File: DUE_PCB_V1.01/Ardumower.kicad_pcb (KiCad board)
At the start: 2 copper layers, 169.3 x 95.5 mm, 81 parts, among them J1 I2C_1, J10 Bumper Left, J11 Bumper Right, J12 P_Left, J13 P_Right, J14 Sonar_R, J15 Sonar_C, J16 Sonar_L, J17 US1, J18 US2, J19 US3, J2 I2C_2, J20 Button, J21 5V IN, J22 Remote, J23 PCB_2, J24 3.3V IN, J25 TX0/RX0, J26 TX1/RX1, J27 TX2/RX2, J28 GPS_TX/GPS_RX, J29 Motor Left, J3 I2C_3, J30 Cutter Motor, J31 Motor Right, J4 DS3231 RTC, J5 9V IN, J6 Drop_Left, J7 Drop_Right, J8 Tilt, J9 Rain, U1 MC33926, U2 MC33926

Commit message: Change D6 and D7
Add Description for PIN D6 and D7 to pinFrontMotorLeft and pinFrontMotorRight
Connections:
- XA1 pad D6: pinFrontMotorLeft -> (no net)
- XA1 pad D7: pinFrontMotorLeft -> (no net)
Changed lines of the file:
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@@
     (zones 0)
     (modules 81)
-    (nets 94)
+    (nets 93)
   )
   (page A4)
@@
   (net 82 DUE_3.3V)
   (net 83 DUE_5V)
-  (net 84 pinFrontMotorLeft)
-  (net 85 "Net-(D3-Pad2)")
-  (net 86 "Net-(J15-Pad3)")
-  (net 87 "Net-(J16-Pad3)")
-  (net 88 "Net-(J21-Pad2)")
-  (net 89 "Net-(J24-Pad2)")
-  (net 90 "Net-(J31-Pad6)")
-  (net 91 "Net-(J31-Pad4)")
-  (net 92 "Net-(J31-Pad1)")
-  (net 93 "Net-(JP3-Pad2)")
+  (net 84 "Net-(D3-Pad2)")
+  (net 85 "Net-(J15-Pad3)")
+  (net 86 "Net-(J16-Pad3)")
+  (net 87 "Net-(J21-Pad2)")
+  (net 88 "Net-(J24-Pad2)")
+  (net 89 "Net-(J31-Pad6)")
+  (net 90 "Net-(J31-Pad4)")
+  (net 91 "Net-(J31-Pad1)")
+  (net 92 "Net-(JP3-Pad2)")
   (net_class Default "This is the default net class."
     (clearance 0.2)
@@
     (add_net pinDropRight)
     (add_net pinFrontMotorLeft)
+    (add_net pinFrontMotorRight)
     (add_net pinLED)
     (add_net pinLawnBackRecv)
@@
       (net 40 pinSonarCenterTrigger))
     (pad 3 thru_hole oval (at 0 5.08) (size 1.7 1.7) (drill 1) (layers *.Cu *.Mask)
-      (net 86 "Net-(J15-Pad3)"))
+      (net 85 "Net-(J15-Pad3)"))
     (pad 2 thru_hole oval (at 0 2.54) (size 1.7 1.7) (drill 1) (layers *.Cu *.Mask)
       (net 3 GND))
@@
     (fp_line (start 7.79 4) (end -2.71 4) (layer F.CrtYd) (width 0.05))
     (pad 2 thru_hole circle (at 5.08 0 90) (size 3 3) (drill 1.52) (layers *.Cu *.Mask)
-      (net 88 "Net-(J21-Pad2)"))
+      (net 87 "Net-(J21-Pad2)"))
     (pad 1 thru_hole rect (at 0 0 90) (size 3 3) (drill 1.52) (layers *.Cu *.Mask)
       (net 3 GND))
@@
     (fp_line (start 7.79 4) (end -2.71 4) (layer F.CrtYd) (width 0.05))
     (pad 2 thru_hole circle (at 5.08 0 90) (size 3 3) (drill 1.52) (layers *.Cu *.Mask)
-      (net 89 "Net-(J24-Pad2)"))
+      (net 88 "Net-(J24-Pad2)"))
     (pad 1 thru_hole rect (at 0 0 90) (size 3 3) (drill 1.52) (layers *.Cu *.Mask)
       (net 3 GND))
@@
     )
     (pad 2 thru_hole oval (at 0 2.54) (size 1.7 1.7) (drill 1) (layers *.Cu *.Mask)
-      (net 93 "Net-(JP3-Pad2)"))
+      (net 92 "Net-(JP3-Pad2)"))
     (pad 1 thru_hole rect (at 0 0) (size 1.7 1.7) (drill 1) (layers *.Cu *.Mask)
       (net 27 pinBuzzer))
@@
     )
     (pad 2 thru_hole oval (at 0 2.54) (size 1.7 1.7) (drill 1) (layers *.Cu *.Mask)
-      (net 92 "Net-(J31-Pad1)"))
+      (net 91 "Net-(J31-Pad1)"))
     (pad 1 thru_hole rect (at 0 0) (size 1.7 1.7) (drill 1) (layers *.Cu *.Mask)
       (net 68 +5VA))
@@
       (net 80 +3V3))
     (pad 1 thru_hole rect (at 0 0) (size 1.7 1.7) (drill 1) (layers *.Cu *.Mask)
-      (net 89 "Net-(J24-Pad2)"))
+      (net 88 "Net-(J24-Pad2)"))
     (model ${KISYS3DMOD}/Connector_PinHeader_2.54mm.3dshapes/PinHeader_1x03_P2.54mm_Vertical.wrl
       (at (xyz 0 0 0))
@@
       (net 81 +5V))
     (pad 1 thru_hole rect (at 0 0) (size 1.7 1.7) (drill 1) (layers *.Cu *.Mask)
-      (net 88 "Net-(J21-Pad2)"))
+      (net 87 "Net-(J21-Pad2)"))
     (model ${KISYS3DMOD}/Connector_PinHeader_2.54mm.3dshapes/PinHeader_1x03_P2.54mm_Vertical.wrl
       (at (xyz 0 0 0))
@@
       (net 8 pinMotorRightPWM))
     (pad 6 thru_hole oval (at -2.54 5.08) (size 1.7 1.7) (drill 1) (layers *.Cu *.Mask)
-      (net 90 "Net-(J31-Pad6)"))
+      (net 89 "Net-(J31-Pad6)"))
     (pad 5 thru_hole oval (at 0 5.08) (size 1.7 1.7) (drill 1) (layers *.Cu *.Mask)
       (net 67 MotorBreak))
     (pad 4 thru_hole oval (at -2.54 2.54) (size 1.7 1.7) (drill 1) (layers *.Cu *.Mask)
-      (net 91 "Net-(J31-Pad4)"))
+      (net 90 "Net-(J31-Pad4)"))
     (pad 3 thru_hole oval (at 0 2.54) (size 1.7 1.7) (drill 1) (layers *.Cu *.Mask)
       (net 10 pinMotorRightDir))
@@
       (net 9 pinMotorEnable))
     (pad 1 thru_hole rect (at 0 0) (size 1.7 1.7) (drill 1) (layers *.Cu *.Mask)
-      (net 92 "Net-(J31-Pad1)"))
+      (net 91 "Net-(J31-Pad1)"))
     (model ${KISYS3DMOD}/Connector_PinSocket_2.54mm.3dshapes/PinSocket_2x04_P2.54mm_Vertical.wrl
       (at (xyz 0 0 0))
@@
       (net 37 pinSonarLeftTrigger))
     (pad 3 thru_hole oval (at 0 5.08) (size 1.7 1.7) (drill 1) (layers *.Cu *.Mask)
-      (net 87 "Net-(J16-Pad3)"))
+      (net 86 "Net-(J16-Pad3)"))
     (pad 2 thru_hole oval (at 0 2.54) (size 1.7 1.7) (drill 1) (layers *.Cu *.Mask)
       (net 3 GND))
@@
       (net 6 pinMotorRightFault))
     (pad 1 thru_hole circle (at 0 0) (size 1.6 1.6) (drill 0.8) (layers *.Cu *.Mask)
-      (net 90 "Net-(J31-Pad6)"))
+      (net 89 "Net-(J31-Pad6)"))
     (model ${KISYS3DMOD}/Resistor_THT.3dshapes/R_Axial_DIN0207_L6.3mm_D2.5mm_P2.54mm_Vertical.wrl
       (at (xyz 0 0 0))
@@
       (net 3 GND))
     (pad 1 thru_hole circle (at 0 0) (size 1.6 1.6) (drill 0.8) (layers *.Cu *.Mask)
-      (net 90 "Net-(J31-Pad6)"))
+      (net 89 "Net-(J31-Pad6)"))
     (model ${KISYS3DMOD}/Resistor_THT.3dshapes/R_Axial_DIN0207_L6.3mm_D2.5mm_P2.54mm_Vertical.wrl
       (at (xyz 0 0 0))
@@
       (net 20 pinOdometryRight))
     (pad 1 thru_hole circle (at 0 0) (size 1.6 1.6) (drill 0.8) (layers *.Cu *.Mask)
-      (net 91 "Net-(J31-Pad4)"))
+      (net 90 "Net-(J31-Pad4)"))
     (model ${KISYS3DMOD}/Resistor_THT.3dshapes/R_Axial_DIN0207_L6.3mm_D2.5mm_P2.54mm_Vertical.wrl
       (at (xyz 0 0 0))
@@
       (net 3 GND))
     (pad 1 thru_hole circle (at 0 0) (size 1.6 1.6) (drill 0.8) (layers *.Cu *.Mask)
-      (net 91 "Net-(J31-Pad4)"))
+      (net 90 "Net-(J31-Pad4)"))
     (model ${KISYS3DMOD}/Resistor_THT.3dshapes/R_Axial_DIN0207_L6.3mm_D2.5mm_P2.54mm_Vertical.wrl
       (at (xyz 0 0 0))
@@
     (fp_arc (start 1.27 0) (end -0.23 -1.16619) (angle 284.3) (layer F.Fab) (width 0.1))
     (pad 2 thru_hole circle (at 2.54 0 270) (size 1.8 1.8) (drill 0.9) (layers *.Cu *.Mask)
-      (net 85 "Net-(D3-Pad2)"))
+      (net 84 "Net-(D3-Pad2)"))
     (pad 1 thru_hole rect (at 0 0 270) (size 1.8 1.8) (drill 0.9) (layers *.Cu *.Mask)
       (net 3 GND))
@@
     (pad GND1 thru_hole oval (at 26.416 -50.8) (size 1.7272 1.7272) (drill 1.016) (layers *.Cu *.Mask)
       (net 3 GND))
-    (pad D7 thru_hole oval (at 45.72 -50.8) (size 1.7272 1.7272) (drill 1.016) (layers *.Cu *.Mask)
-      (net 84 pinFrontMotorLeft))
-    (pad D6 thru_hole oval (at 48.26 -50.8) (size 1.7272 1.7272) (drill 1.016) (layers *.Cu *.Mask)
-      (net 84 pinFrontMotorLeft))
+    (pad D7 thru_hole oval (at 45.72 -50.8) (size 1.7272 1.7272) (drill 1.016) (layers *.Cu *.Mask))
+    (pad D6 thru_hole oval (at 48.26 -50.8) (size 1.7272 1.7272) (drill 1.016) (layers *.Cu *.Mask))
     (pad D5 thru_hole oval (at 50.8 -50.8) (size 1.7272 1.7272) (drill 1.016) (layers *.Cu *.Mask)
       (net 13 pinMotorLeftPWM))
@@
       (net 3 GND))
     (pad 2 thru_hole circle (at 3.79984 0 270) (size 2 2) (drill 1.00076) (layers *.Cu *.Mask F.SilkS)
-      (net 93 "Net-(JP3-Pad2)"))
+      (net 92 "Net-(JP3-Pad2)"))
     (model ${KISYS3DMOD}/Buzzers_Beepers.3dshapes/Buzzer_12x9.5RM7.6.wrl
       (at (xyz 0 0 0))
@@
       (net 80 +3V3))
     (pad 1 thru_hole circle (at 0 0) (size 1.6 1.6) (drill 0.8) (layers *.Cu *.Mask)
-      (net 85 "Net-(D3-Pad2)"))
+      (net 84 "Net-(D3-Pad2)"))
     (model ${KISYS3DMOD}/Resistor_THT.3dshapes/R_Axial_DIN0207_L6.3mm_D2.5mm_P2.54mm_Vertical.wrl
       (at (xyz 0 0 0))
@@
       (net 3 GND))
     (pad 1 thru_hole circle (at 0 0 270) (size 1.6 1.6) (drill 0.8) (layers *.Cu *.Mask)
-      (net 87 "Net-(J16-Pad3)"))
+      (net 86 "Net-(J16-Pad3)"))
     (model ${KISYS3DMOD}/Resistor_THT.3dshapes/R_Axial_DIN0207_L6.3mm_D2.5mm_P2.54mm_Vertical.wrl
       (at (xyz 0 0 0))
@@
       (net 3 GND))
     (pad 1 thru_hole circle (at 0 0 90) (size 1.6 1.6) (drill 0.8) (layers *.Cu *.Mask)
-      (net 86 "Net-(J15-Pad3)"))
+      (net 85 "Net-(J15-Pad3)"))
     (model ${KISYS3DMOD}/Resistor_THT.3dshapes/R_Axial_DIN0207_L6.3mm_D2.5mm_P2.54mm_Vertical.wrl
       (at (xyz 0 0 0))
@@
       (net 35 pinSonarLeftEcho))
     (pad 1 thru_hole circle (at 0 0 90) (size 1.6 1.6) (drill 0.8) (layers *.Cu *.Mask)
-      (net 87 "Net-(J16-Pad3)"))
+      (net 86 "Net-(J16-Pad3)"))
     (model ${KISYS3DMOD}/Resistor_THT.3dshapes/R_Axial_DIN0207_L6.3mm_D2.5mm_P2.54mm_Vertical.wrl
       (at (xyz 0 0 0))
@@
       (net 41 pinSonarCenterEcho))
     (pad 1 thru_hole circle (at 0 0 270) (size 1.6 1.6) (drill 0.8) (layers *.Cu *.Mask)
-      (net 86 "Net-(J15-Pad3)"))
+      (net 85 "Net-(J15-Pad3)"))
     (model ${KISYS3DMOD}/Resistor_THT.3dshapes/R_Axial_DIN0207_L6.3mm_D2.5mm_P2.54mm_Vertical.wrl
       (at (xyz 0 0 0))

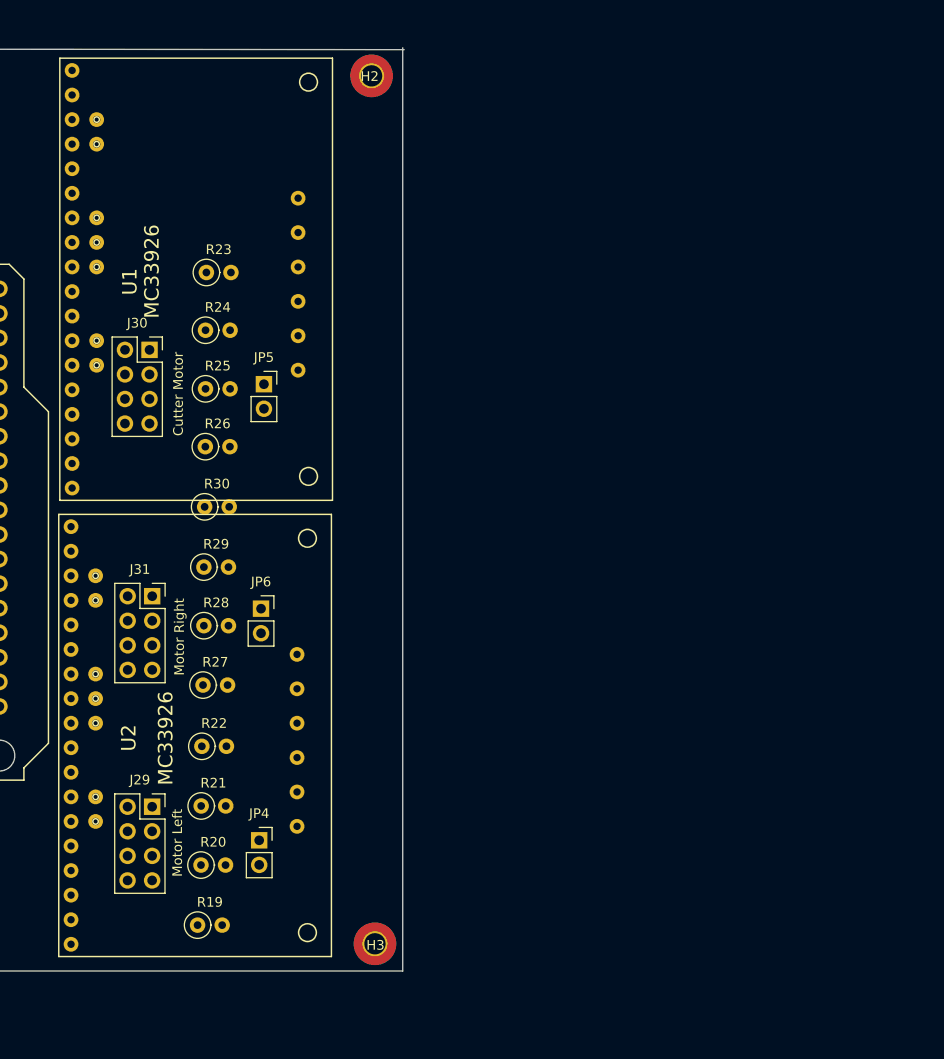
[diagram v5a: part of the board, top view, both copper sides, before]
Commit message: Add new Connectors for 4 Mow Motors and Odometrie
Add new Connectors for 4 Mow Motors and Odometrie
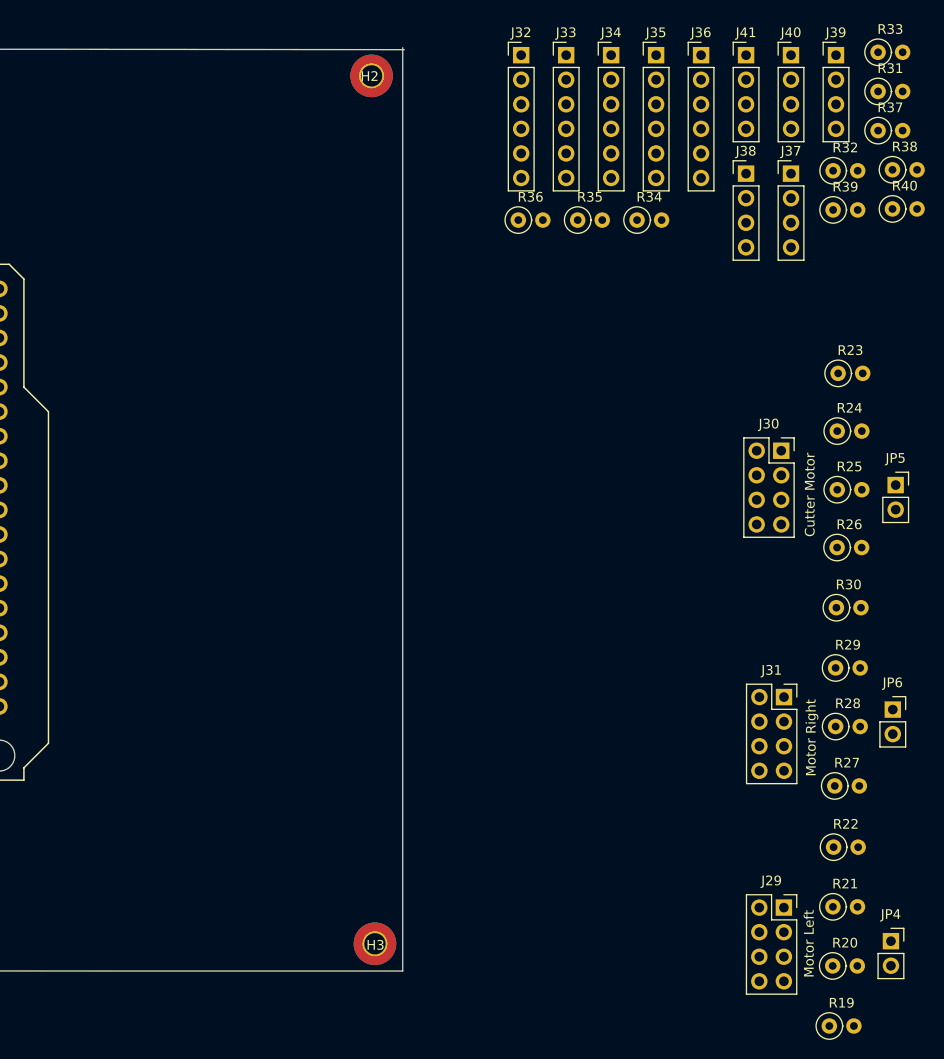
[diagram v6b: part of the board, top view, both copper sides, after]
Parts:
- removed U1, U2: MC33926, Zimprich:MC_33926_31polig_mit_Bohrloch_neue_Masse
- added J32: Motor_Right1, Connector_PinHeader_2.54mm:PinHeader_1x06_P2.54mm_Vertical, F.Cu at (220.6, 36.2)
- added J33: Motor_Right2, Connector_PinHeader_2.54mm:PinHeader_1x06_P2.54mm_Vertical, F.Cu at (225.2, 36.2)
- added J34: Motor_Left1, Connector_PinHeader_2.54mm:PinHeader_1x06_P2.54mm_Vertical, F.Cu at (229.9, 36.2)
- added J35: Motor_Left2, Connector_PinHeader_2.54mm:PinHeader_1x06_P2.54mm_Vertical, F.Cu at (234.5, 36.2)
- added J36: Cutter_Motor, Connector_PinHeader_2.54mm:PinHeader_1x06_P2.54mm_Vertical, F.Cu at (239.2, 36.2)
- added J37: ODORight1, Connector_PinHeader_2.54mm:PinHeader_1x04_P2.54mm_Vertical, F.Cu at (248.5, 48.5)
- added J38: ODORight2, Connector_PinHeader_2.54mm:PinHeader_1x04_P2.54mm_Vertical, F.Cu at (243.8, 48.5)
- added J39: ODOLeft1, Connector_PinHeader_2.54mm:PinHeader_1x04_P2.54mm_Vertical, F.Cu at (253.1, 36.2)
- added J40: ODOLeft2, Connector_PinHeader_2.54mm:PinHeader_1x04_P2.54mm_Vertical, F.Cu at (248.5, 36.2)
- added J41: ODOCutter, Connector_PinHeader_2.54mm:PinHeader_1x04_P2.54mm_Vertical, F.Cu at (243.8, 36.2)
- added R31: 1KO, Resistor_THT:R_Axial_DIN0207_L6.3mm_D2.5mm_P2.54mm_Vertical, F.Cu at (257.5, 40.0)
- added R32: 1KO, Resistor_THT:R_Axial_DIN0207_L6.3mm_D2.5mm_P2.54mm_Vertical, F.Cu at (252.8, 48.2)
- added R33: 1KO, Resistor_THT:R_Axial_DIN0207_L6.3mm_D2.5mm_P2.54mm_Vertical, F.Cu at (257.5, 36.0)
- added R34: 1KO, Resistor_THT:R_Axial_DIN0207_L6.3mm_D2.5mm_P2.54mm_Vertical, F.Cu at (232.6, 53.3)
- added R35: 1KO, Resistor_THT:R_Axial_DIN0207_L6.3mm_D2.5mm_P2.54mm_Vertical, F.Cu at (226.4, 53.3)
- added R36: 1.5KO, Resistor_THT:R_Axial_DIN0207_L6.3mm_D2.5mm_P2.54mm_Vertical, F.Cu at (220.3, 53.3)
- added R37: 1.5KO, Resistor_THT:R_Axial_DIN0207_L6.3mm_D2.5mm_P2.54mm_Vertical, F.Cu at (257.5, 44.0)
- added R38: 1.5KO, Resistor_THT:R_Axial_DIN0207_L6.3mm_D2.5mm_P2.54mm_Vertical, F.Cu at (259.0, 48.1)
- added R39: 1.5KO, Resistor_THT:R_Axial_DIN0207_L6.3mm_D2.5mm_P2.54mm_Vertical, F.Cu at (252.8, 52.2)
- added R40: 1.5KO, Resistor_THT:R_Axial_DIN0207_L6.3mm_D2.5mm_P2.54mm_Vertical, F.Cu at (259.0, 52.1)
- moved R20 66.1 mm to (252.8, 130.4)
- moved R23 66.1 mm to (253.4, 69.2)
- moved R24 66.1 mm to (253.3, 75.1)
- moved R25 66.1 mm to (253.3, 81.2)
- moved J29 66.1 mm to (247.8, 124.4)
- moved J30 66.1 mm to (247.5, 77.2)
- moved J31 66.1 mm to (247.8, 102.6)
- moved JP4 66.1 mm to (258.8, 127.9)
- moved JP5 66.1 mm to (259.3, 80.7)
- moved JP6 66.1 mm to (259.0, 103.9)
- moved R19 66.1 mm to (252.4, 136.6)
- moved R21 66.1 mm to (252.8, 124.3)
- moved R22 66.1 mm to (252.9, 118.1)
- moved R26 66.1 mm to (253.2, 87.2)
- moved R27 66.1 mm to (253.0, 111.8)
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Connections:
- XA1 pad A0: pinMotorRightSense -> (no net)
- XA1 pad A1: pinMotorLeftSense -> (no net)
- XA1 pad A3: pinMotorMowSense -> (no net)
- XA1 pad CANT: (no net) -> pinOdometryRight2
- XA1 pad D6: (no net) -> pinMotorLeft2PWM
- XA1 pad D7: (no net) -> pinMotorRight2PWM
- XA1 pad DAC1: (no net) -> pinOdometryLeft2
